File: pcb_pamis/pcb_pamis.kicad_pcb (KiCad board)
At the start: 2 copper layers, 53 parts, among them J1 USB_A, J10 Conn_01x03, J11 Conn_01x03, J12 Conn_02x06_Odd_Even, J2 1755736, J3 Conn_01x04, J4 Conn_01x04, J5 Conn_01x04, J6 Conn_01x05, J7 Conn_01x05, J8 Conn_01x05, J9 Conn_01x03, Q1 Q_NPN_BEC, Q2 Q_NPN_BEC, SW1 SW_Push, U1 ESP32-WROOM-32UE, U2 CP2102N-Axx-xQFN28, U3 TMC2209_SILENTSTEPSTICK, U4 TMC2209_SILENTSTEPSTICK, U5 TMC2209_SILENTSTEPSTICK

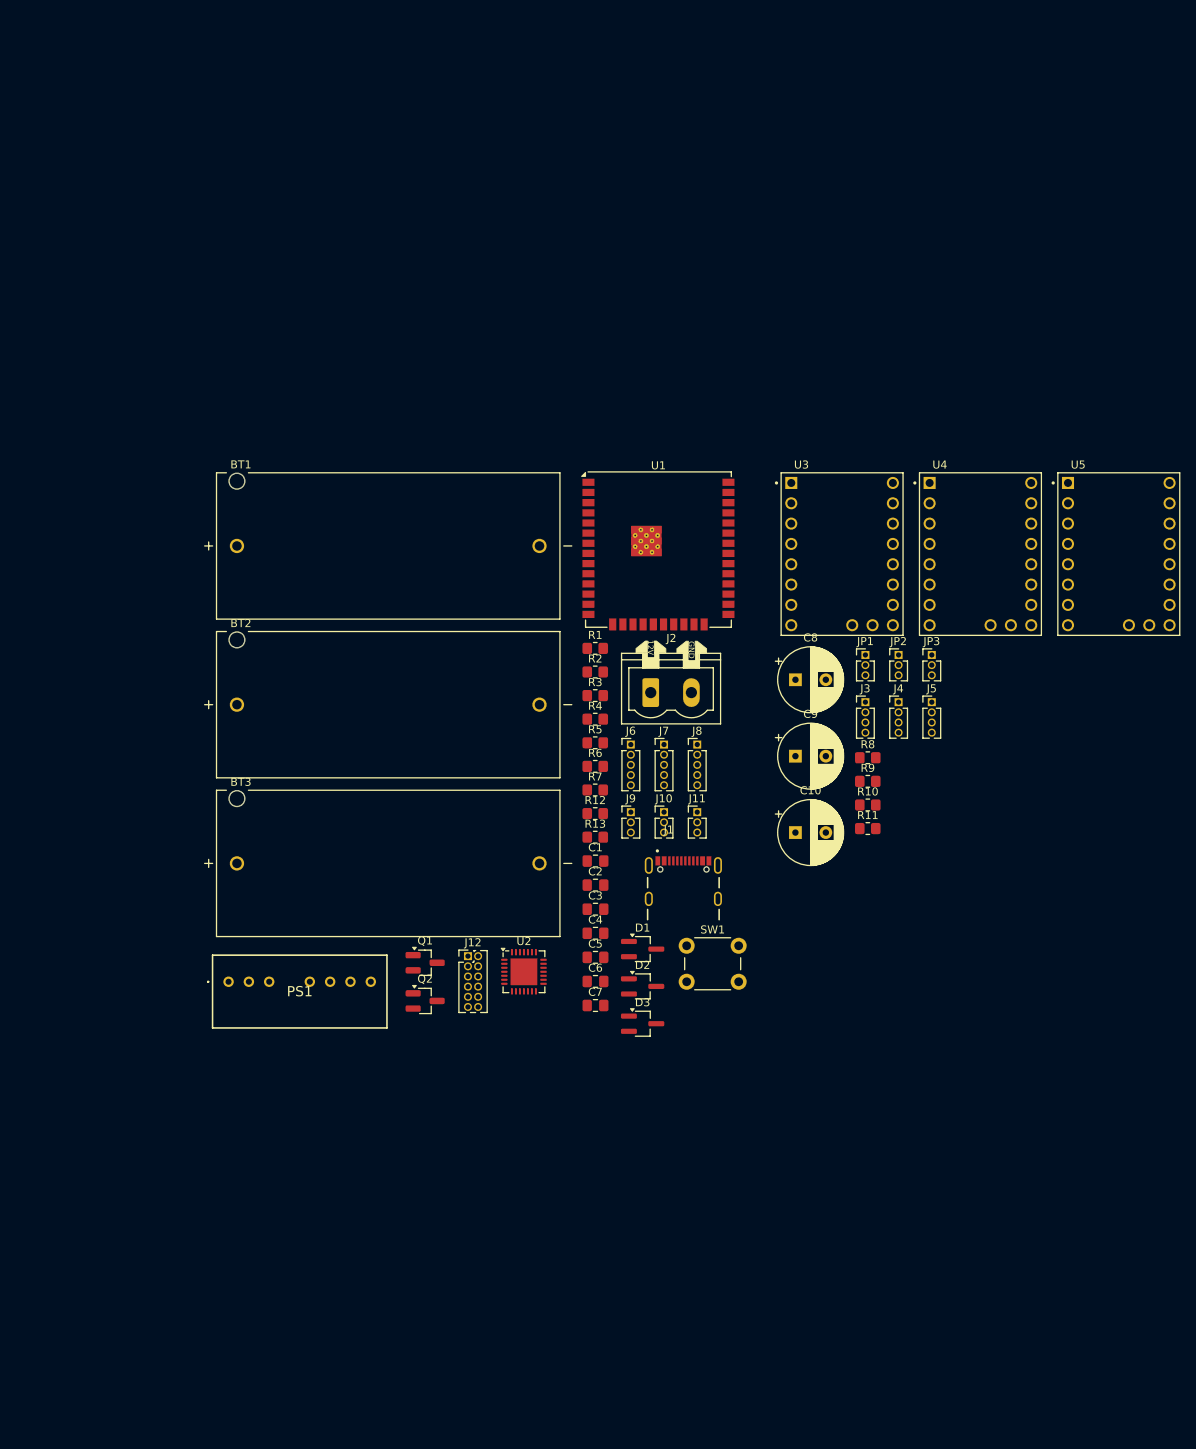
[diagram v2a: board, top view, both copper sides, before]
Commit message: correction symbole type C
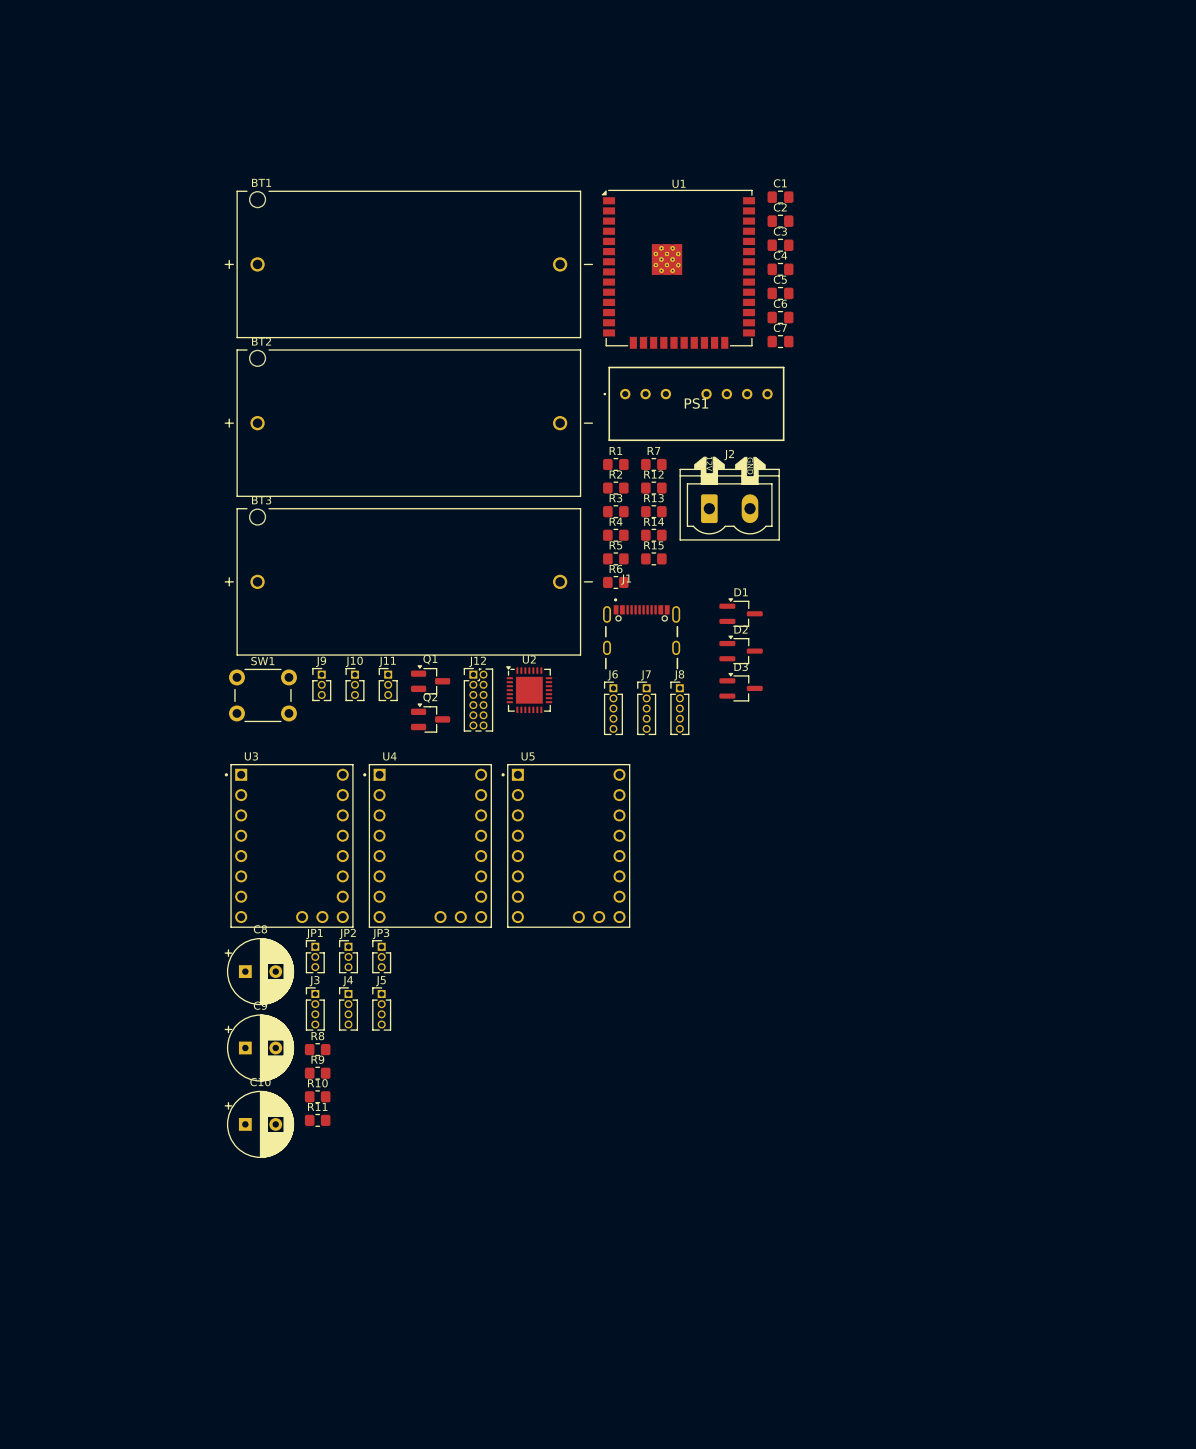
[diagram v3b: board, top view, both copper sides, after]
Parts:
- added R14: 5,1k, Resistor_SMD:R_0805_2012Metric_Pad1.20x1.40mm_HandSolder, F.Cu at (140.6, 83.2)
- added R15: 5,1k, Resistor_SMD:R_0805_2012Metric_Pad1.20x1.40mm_HandSolder, F.Cu at (140.6, 86.2)
- J1: value USB_A -> USB_C_Receptacle_USB2.0_16P
- moved PS1 88.6 mm to (137.1, 65.6)
- moved C1 86.2 mm to (156.5, 40.9)
- moved C4 86.2 mm to (156.5, 50.0)
- moved C5 86.2 mm to (156.5, 53.0)
- moved C7 86.2 mm to (156.5, 59.0)
- moved C2 86.2 mm to (156.5, 44.0)
- moved C3 86.2 mm to (156.5, 47.0)
- moved C6 86.2 mm to (156.5, 56.0)
- moved C9 77.8 mm to (89.6, 147.3)
- moved J5 77.8 mm to (106.6, 140.6)
- moved U4 77.8 mm to (112.7, 122.0)
- moved C10 77.8 mm to (89.6, 156.8)
- moved C8 77.8 mm to (89.6, 137.8)
- moved J3 77.8 mm to (98.3, 140.6)
- moved J4 77.8 mm to (102.5, 140.6)
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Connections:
- J1 pad A5: NC_2 -> Net-(J1-CC1)
- J1 pad A8: NC_1 -> unconnected-(J1-SBU1-PadA8)
- J1 pad B5: NC_3 -> Net-(J1-CC2)
- J1 pad B8: NC -> unconnected-(J1-SBU2-PadB8)

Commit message: wip: placement composants
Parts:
- R4, R5: moved to B.Cu
- moved C1 78.3 mm to (167.5, 118.5)
- moved C2 78.3 mm to (167.5, 121.5)
- moved J1 65.4 mm to (143.7, 32.0), turned to 180 degrees
- moved U1 60.6 mm to (107.0, 98.0)
- moved D2 54.3 mm to (154.4, 151.9)
- moved J2 54.3 mm to (150.5, 134.1)
- moved R13 54.3 mm to (143.5, 134.5)
- moved D3 54.3 mm to (154.4, 156.6)
- moved R12 54.3 mm to (143.5, 131.5)
- moved D1 54.3 mm to (154.4, 147.2)
- moved U2 54.2 mm to (143.6, 51.6), turned to -90 degrees
- moved Q2 46.7 mm to (147.1, 74.5), turned to -90 degrees
- moved R15 45.2 mm to (141.5, 41.0), turned to -90 degrees
- moved R14 42.4 mm to (145.0, 41.0), turned to -90 degrees
- moved BT3 41.3 mm to (126.0, 51.0), turned to 90 degrees
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
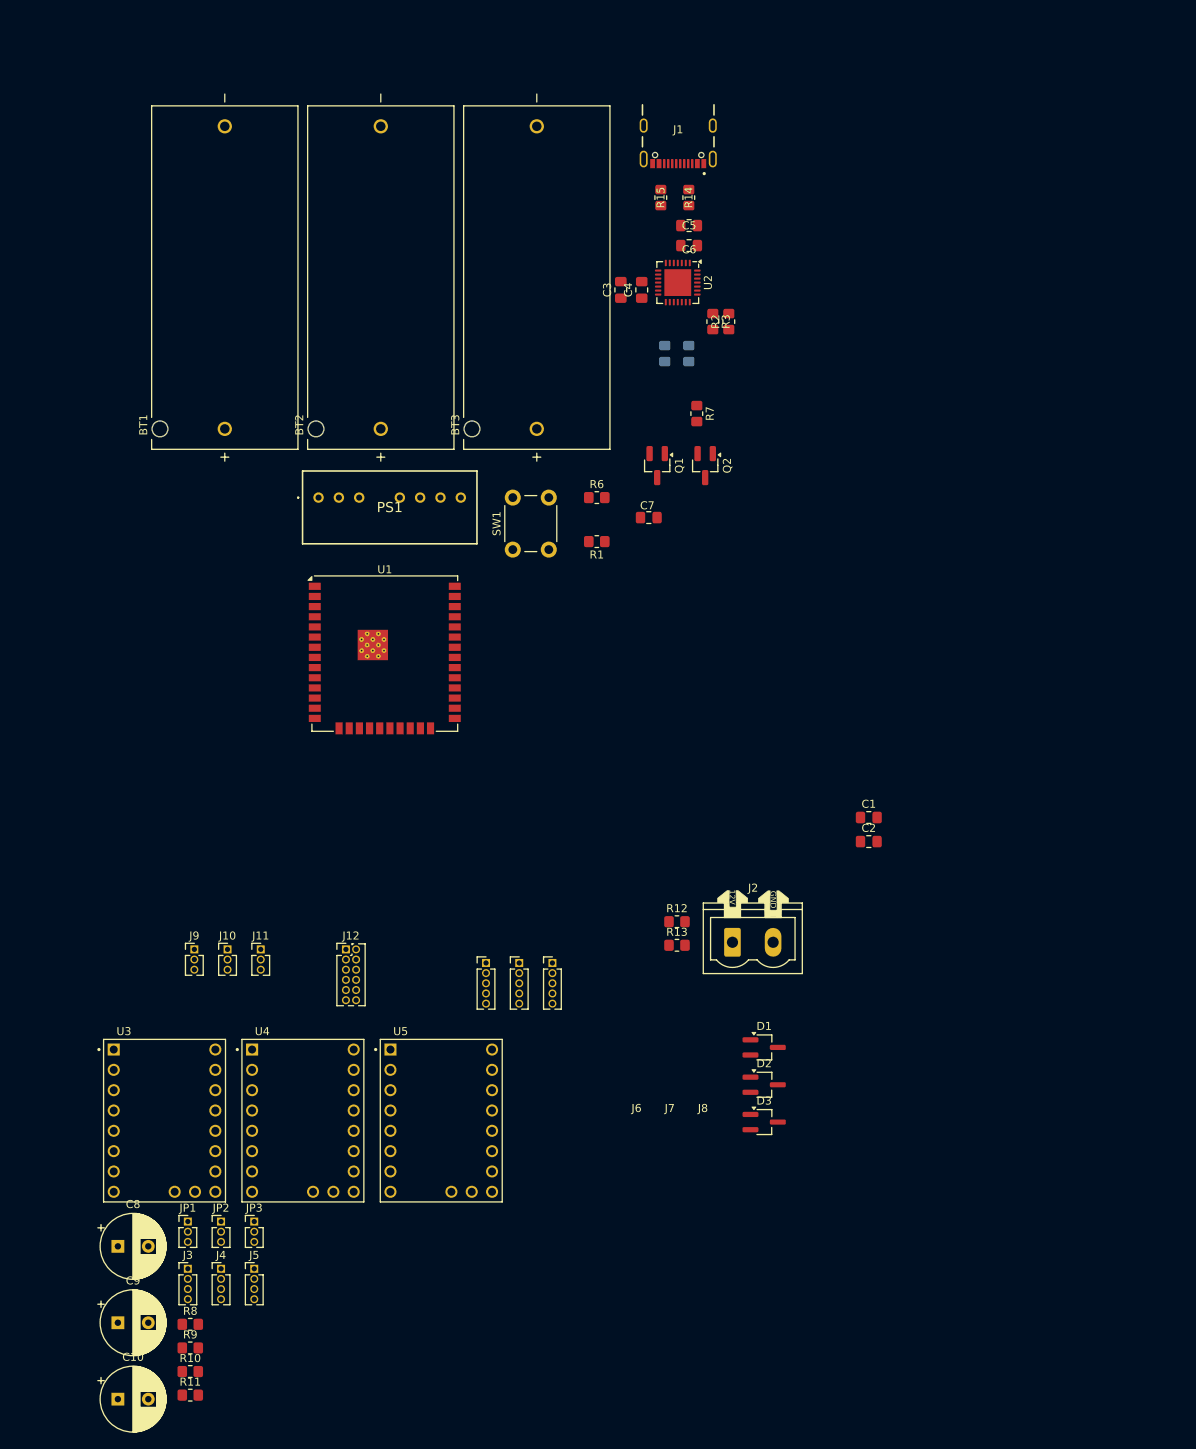
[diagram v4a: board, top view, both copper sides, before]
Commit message: premier placement des composants sur le pcb PAMI
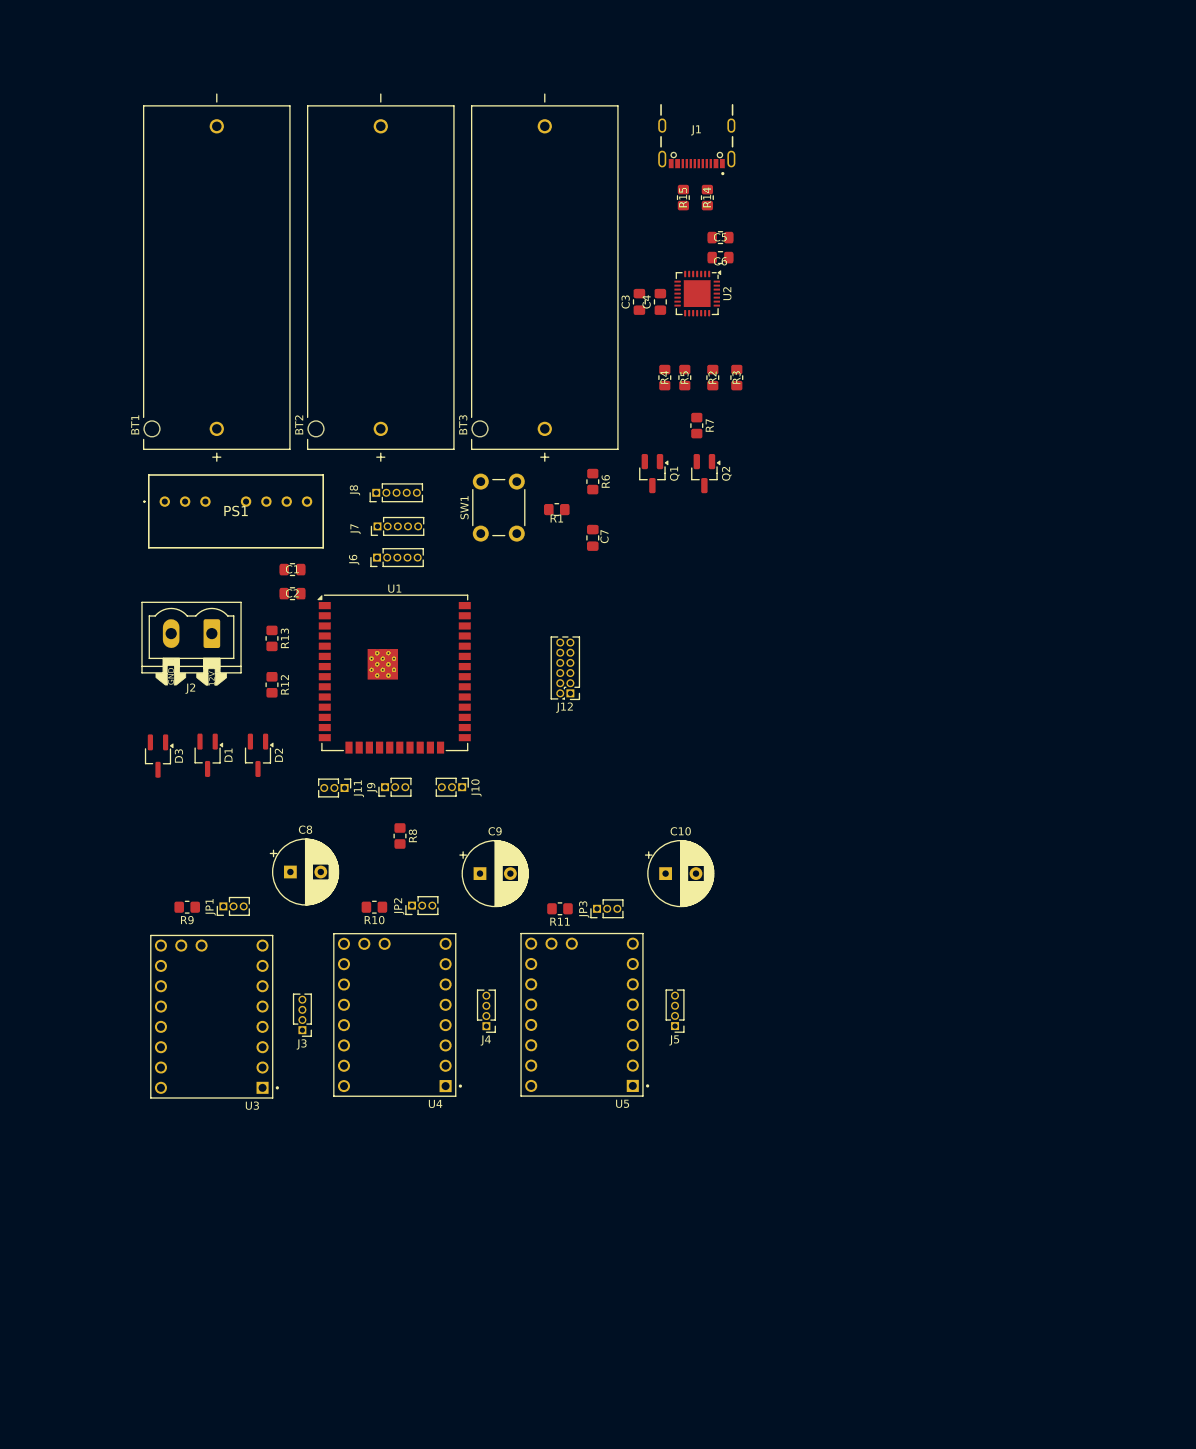
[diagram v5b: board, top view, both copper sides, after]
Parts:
- R4, R5: moved to F.Cu
- moved C10 94.9 mm to (142.1, 125.5)
- moved D3 88.5 mm to (78.7, 110.8), turned to -90 degrees
- moved D1 78.6 mm to (84.8, 110.7), turned to -90 degrees
- moved C1 78.4 mm to (95.5, 87.5)
- moved C2 78.4 mm to (95.5, 90.5)
- moved R11 76.4 mm to (128.9, 129.9), turned to 180 degrees
- moved J2 75.7 mm to (85.4, 95.5), turned to 180 degrees
- moved D2 75.5 mm to (91.2, 110.7), turned to -90 degrees
- moved C9 72.1 mm to (118.9, 125.5)
- moved R8 66.4 mm to (108.9, 120.8), turned to -90 degrees
- moved R13 63.5 mm to (92.9, 96.1), turned to -90 degrees
- moved J8 62.8 mm to (105.9, 77.9), turned to 90 degrees
- moved R10 62.4 mm to (105.7, 129.7), turned to 180 degrees
- moved J5 60.7 mm to (143.3, 144.6), turned to 180 degrees
- moved R12 58.6 mm to (92.9, 101.9), turned to -90 degrees
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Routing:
- net RX_MOTEUR: track 0.00 -> 0.53 mm
- net EN: track 0.00 -> 0.50 mm

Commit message: plan de masse sur pcb pamis et ajout projet pcb actionneurs
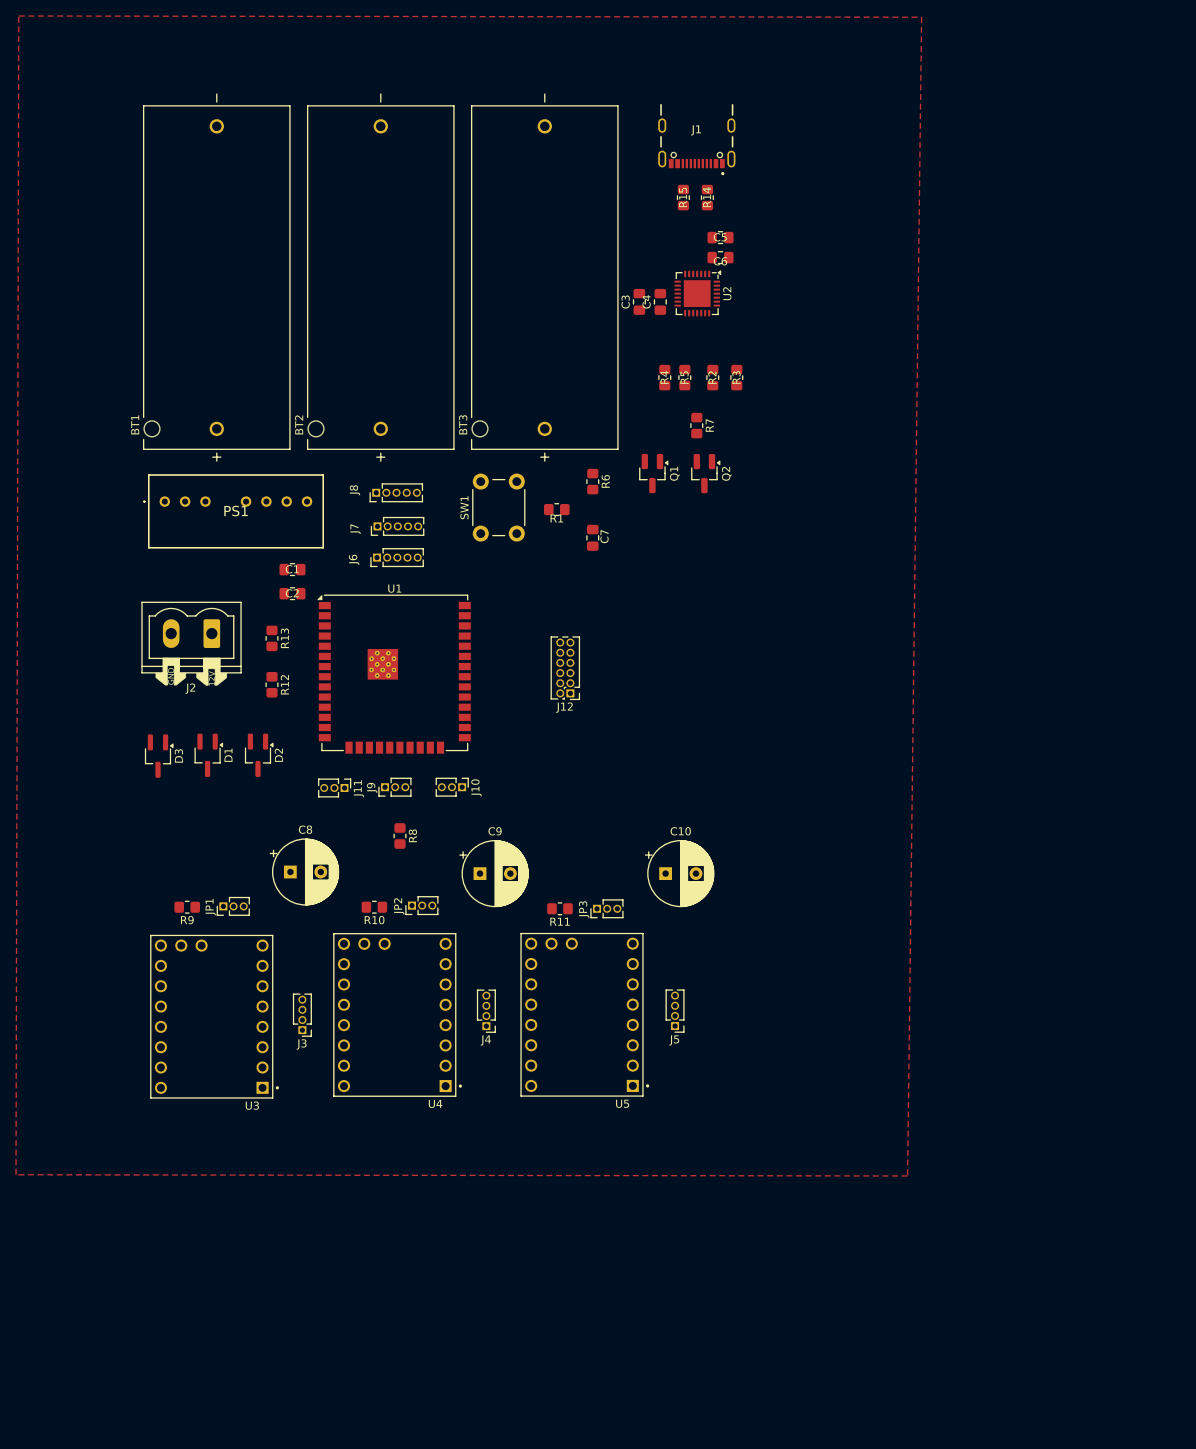
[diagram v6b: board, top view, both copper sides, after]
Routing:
- added copper zone on F.Cu, net GND
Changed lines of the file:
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@@
 		(net 62)
+	)
+	(zone
+		(net 5)
+		(net_name "GND")
+		(layer "F.Cu")
+		(hatch edge 0.5)
+		(connect_pads
+			(clearance 0.5)
+		)
+		(min_thickness 0.25)
+		(filled_areas_thickness no)
+		(fill yes
+			(thermal_gap 0.5)
+			(thermal_bridge_width 0.5)
+		)
+		(polygon
+			(pts
+				(xy 61.25 18.3) (xy 174.1 18.45) (xy 172.35 163.3) (xy 60.9 163.15)
+			)
+		)
 	)
 	(embedded_fonts no)
